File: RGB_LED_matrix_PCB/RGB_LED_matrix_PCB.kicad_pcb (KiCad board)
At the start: 2 copper layers, 100 x 100 mm, 215 parts, among them CN1 B03B-XASK-1-A(LF)(SN), U1 WS2815F, U10 WS2815F, U100 WS2815F, U11 WS2815F, U12 WS2815F, U13 WS2815F, U14 WS2815F, U15 WS2815F, U16 WS2815F, U17 WS2815F, U18 WS2815F, U19 WS2815F, U2 WS2815F, U20 WS2815F, U21 WS2815F, U22 WS2815F, U23 WS2815F, U24 WS2815F, U25 WS2815F, U26 WS2815F, U27 WS2815F, U28 WS2815F, U29 WS2815F, U3 WS2815F, U30 WS2815F, U31 WS2815F, U32 WS2815F, U33 WS2815F, U34 WS2815F, U35 WS2815F, U36 WS2815F, U37 WS2815F, U38 WS2815F, U39 WS2815F, U4 WS2815F, U40 WS2815F, U41 WS2815F, U42 WS2815F, U43 WS2815F, U44 WS2815F, U45 WS2815F, U46 WS2815F, U47 WS2815F, U48 WS2815F, U49 WS2815F, U5 WS2815F, U50 WS2815F, U51 WS2815F, U52 WS2815F, U53 WS2815F, U54 WS2815F, U55 WS2815F, U56 WS2815F, U57 WS2815F, U58 WS2815F, U59 WS2815F, U6 WS2815F, U60 WS2815F, U61 WS2815F, U62 WS2815F, U63 WS2815F, U64 WS2815F, U65 WS2815F, U66 WS2815F, U67 WS2815F, U68 WS2815F, U69 WS2815F, U7 WS2815F, U70 WS2815F, U71 WS2815F, U72 WS2815F, U73 WS2815F, U74 WS2815F, U75 WS2815F, U76 WS2815F, U77 WS2815F, U78 WS2815F, U79 WS2815F, U8 WS2815F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

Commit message: Finished the LED matrix board layout - it just needs some polishing now and minor fixes
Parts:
- added REF**: Screw_Generic_2.0x3.0mm_SilkScreen, Symbol:Screw_Generic_2.0x3.0mm_SilkScreen, B.Cu at (174.0, 127.0)
- added REF**: Screw_Generic_2.0x3.0mm_SilkScreen, Symbol:Screw_Generic_2.0x3.0mm_SilkScreen, B.Cu at (174.0, 67.0)
- added REF**: Screw_Generic_2.0x3.0mm_SilkScreen, Symbol:Screw_Generic_2.0x3.0mm_SilkScreen, B.Cu at (114.0, 127.0)
- added REF**: Screw_Generic_2.0x3.0mm_SilkScreen, Symbol:Screw_Generic_2.0x3.0mm_SilkScreen, B.Cu at (114.0, 67.0)
- added TP10: +12V, TestPoint:TestPoint_Pad_D1.0mm, F.Cu at (195.5, 118.5)
- added TP11: +12V, TestPoint:TestPoint_Pad_D1.0mm, F.Cu at (100.5, 138.5)
- added TP12: +12V, TestPoint:TestPoint_Pad_D1.0mm, F.Cu at (195.5, 138.5)
- added TP3: +12V, TestPoint:TestPoint_Pad_D1.0mm, F.Cu at (100.5, 58.5)
- added TP4: +12V, TestPoint:TestPoint_Pad_D1.0mm, F.Cu at (195.5, 58.5)
- added TP5: +12V, TestPoint:TestPoint_Pad_D1.0mm, F.Cu at (100.5, 78.5)
- added TP6: +12V, TestPoint:TestPoint_Pad_D1.0mm, F.Cu at (195.5, 78.5)
- added TP7: +12V, TestPoint:TestPoint_Pad_D1.0mm, F.Cu at (100.5, 98.5)
- added TP8: +12V, TestPoint:TestPoint_Pad_D1.0mm, F.Cu at (195.5, 98.5)
- added TP9: +12V, TestPoint:TestPoint_Pad_D1.0mm, F.Cu at (100.5, 118.5)
- C101, C102, C103, C104, C105, C106, C107, C108, C109, C110, TP1, TP2: moved to B.Cu
- moved C110 162.4 mm to (122.0, 137.0), turned to 180 degrees
- moved C108 160.7 mm to (122.0, 117.0), turned to 180 degrees
- moved C106 159.1 mm to (122.0, 97.0), turned to 180 degrees
- moved C104 139.2 mm to (121.7, 77.0), turned to 180 degrees
- moved C102 138.5 mm to (122.0, 57.0), turned to 180 degrees
- moved TP1 133.7 mm to (194.8, 142.0), turned to 180 degrees
- moved TP2 133.0 mm to (192.1, 142.0), turned to 180 degrees
- moved C109 123.3 mm to (172.0, 137.0), turned to 180 degrees
- moved C107 120.7 mm to (172.0, 117.0), turned to 180 degrees
- moved C105 92.2 mm to (172.0, 97.0), turned to 180 degrees
- moved C103 91.0 mm to (172.0, 77.0), turned to 180 degrees
- moved C101 90.0 mm to (172.0, 57.0), turned to 180 degrees
- moved CN1 23.4 mm to (185.6, 88.3), turned to 180 degrees
- moved R1 11.5 mm to (196.1, 53.0), turned to 90 degrees
- moved C80 7.78 mm to (188.9, 125.9), turned to 0 degrees
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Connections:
- CN1 pad 1: +12V -> GND
- CN1 pad 3: GND -> +12V
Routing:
- net Net-(CN1-Pad2): track 0.00 -> 50.2 mm, vias 0 -> 1
- net +12V: track 628.5 -> 603.5 mm, vias 0 -> 429
- net /LED_ROW8/DOUT2: track 5.20 -> 22.8 mm, vias 0 -> 2
- net /LED_ROW6/DOUT2: track 5.20 -> 22.8 mm, vias 0 -> 2
- net /LED_ROW4/DOUT2: track 5.20 -> 22.8 mm, vias 0 -> 2
- net /LED_ROW2/DOUT2: track 5.20 -> 22.8 mm, vias 0 -> 2
- net /LED_ROW/DOUT2: track 5.20 -> 22.8 mm, vias 0 -> 2
- net /LED_ROW1/DOUT1: track 14.4 -> 30.7 mm
- net /LED_ROW7/DOUT1: track 14.4 -> 30.7 mm
- net /LED_ROW5/DOUT1: track 14.4 -> 30.7 mm
- net /LED_ROW3/DOUT1: track 14.4 -> 30.3 mm
- net /LED_ROW1/DOUT2: track 5.20 -> 18.4 mm
- net /LED_ROW7/DOUT2: track 5.20 -> 18.4 mm
- net /LED_ROW5/DOUT2: track 5.20 -> 18.4 mm
- net /LED_ROW3/DOUT2: track 5.20 -> 18.4 mm
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- added copper zone on B.Cu, net +12V

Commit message: Made some slight modyfications to the RGB LED matrix layout.
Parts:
- moved R1 0.20 mm to (195.9, 53.0)
- moved C30 0.20 mm to (98.2, 71.4)
- moved C50 0.20 mm to (98.2, 91.4)
- moved C70 0.20 mm to (98.2, 111.4)
- moved C90 0.20 mm to (98.2, 131.4)
- moved C100 0.20 mm to (195.8, 142.6)
- moved C10 0.10 mm to (98.1, 51.4)
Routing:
- net +12V: track 603.5 -> 602.4 mm
- net GND: vias 303 -> 463
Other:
- board size 100 x 100 mm -> 99.5 x 99.5 mm

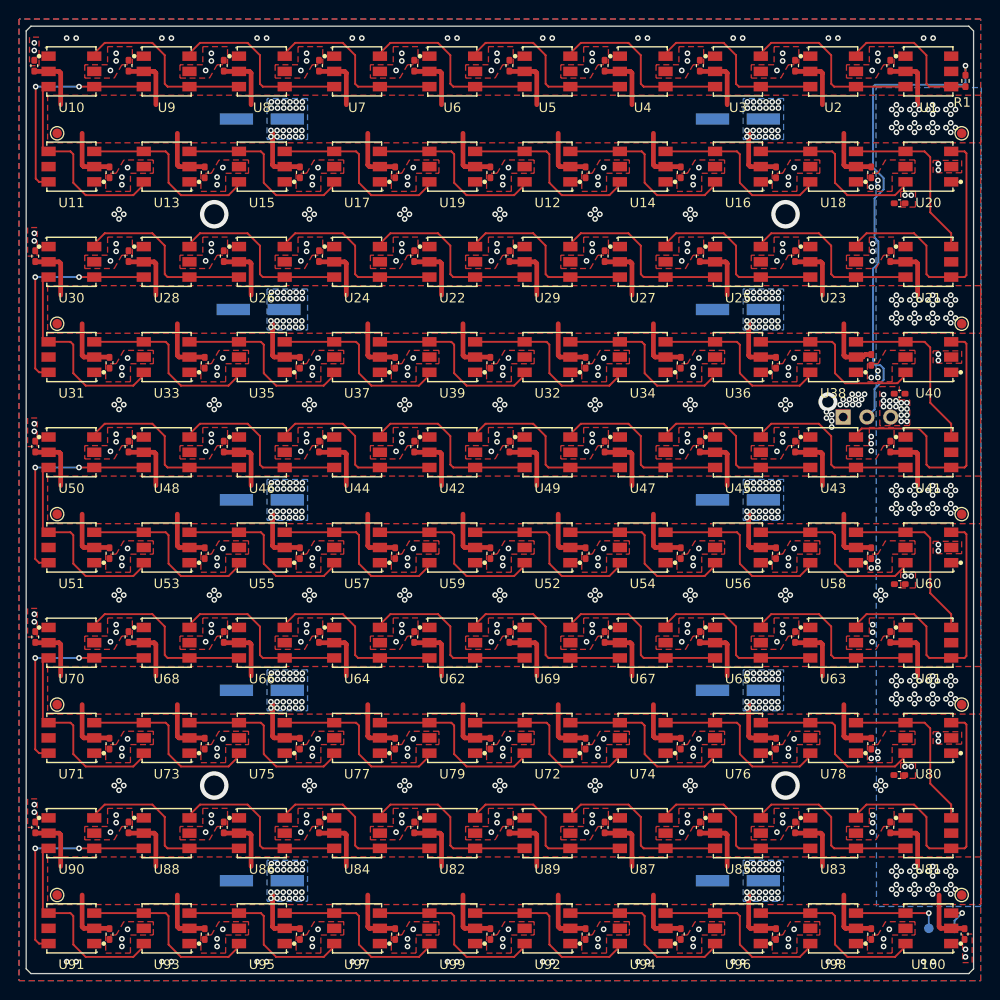
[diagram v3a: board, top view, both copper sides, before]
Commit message: Fixed silkscreen and added extra capacitor row in a new design variant in LED matrix PCB.
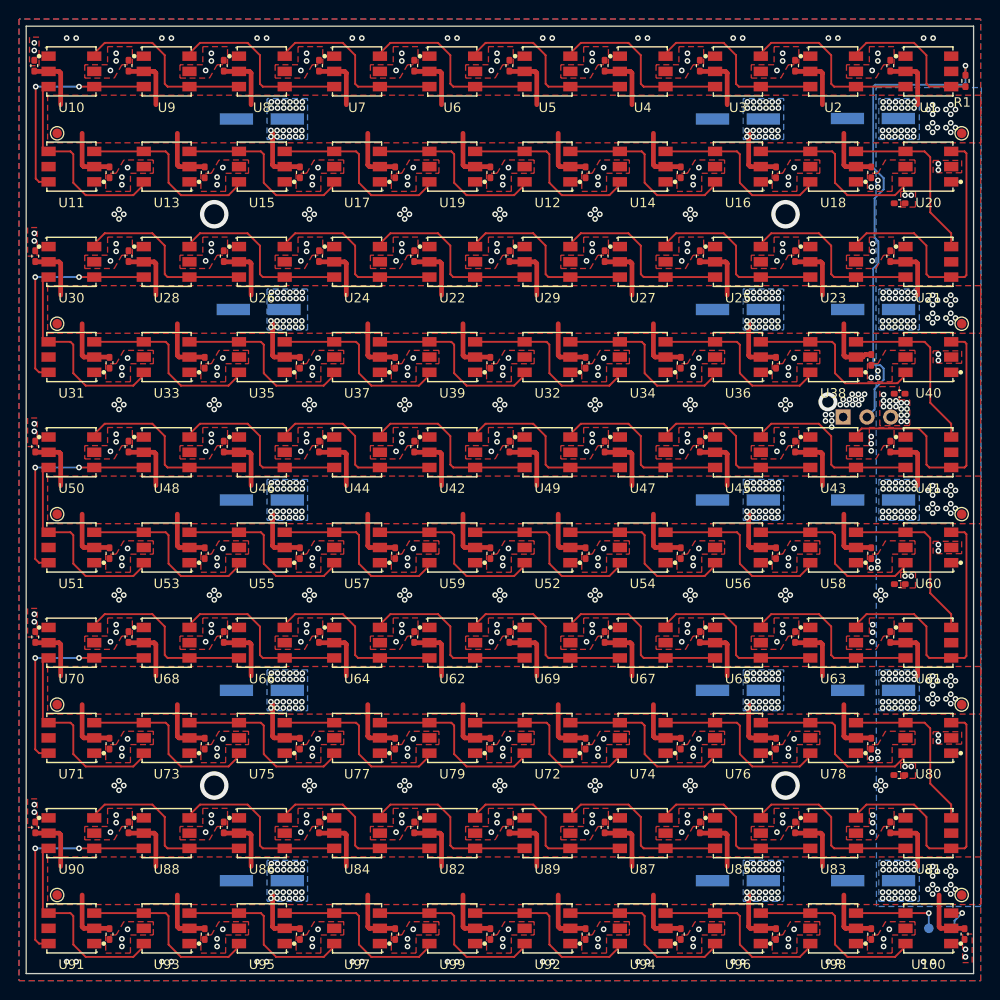
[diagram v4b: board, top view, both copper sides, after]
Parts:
- removed kibuzzard-6A877ACD: G***, kibuzzard-6A877ACD
- added C111: 100uF, lcsc_footprints:C19673858_CAP-SMD_BD6_3-L6_5-W6_5-LS7_2-FD_1, B.Cu at (186.2, 57.0)
- added C112: 100uF, lcsc_footprints:C19673858_CAP-SMD_BD6_3-L6_5-W6_5-LS7_2-FD_1, B.Cu at (186.2, 77.0)
- added C113: 100uF, lcsc_footprints:C19673858_CAP-SMD_BD6_3-L6_5-W6_5-LS7_2-FD_1, B.Cu at (186.2, 97.0)
- added C114: 100uF, lcsc_footprints:C19673858_CAP-SMD_BD6_3-L6_5-W6_5-LS7_2-FD_1, B.Cu at (186.2, 117.0)
- added C115: 100uF, lcsc_footprints:C19673858_CAP-SMD_BD6_3-L6_5-W6_5-LS7_2-FD_1, B.Cu at (186.2, 137.0)
- added G***: LOGO, LOGO, B.Cu at (142.3, 96.4)
- added kibuzzard-6AA54A1E: G***, kibuzzard-6AA54A1E, B.Cu at (172.2, 87.2)
- C101, C102, C103, C104, C105, C106, C107, C108, C109, C110: value RZE-35V101MF80UQ-R2 -> 100uF
- moved REF** 0.70 mm to (173.3, 127.0), turned to -90 degrees
- moved REF** 0.65 mm to (173.3, 67.0), turned to -90 degrees
- moved REF** 0.55 mm to (113.5, 67.0), turned to -90 degrees
- moved REF** 0.46 mm to (113.5, 126.9), turned to -90 degrees
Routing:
- net +12V: vias 429 -> 469
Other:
- outline, holes or cut-outs redrawn
- board text added: "-... ..- -.-."
